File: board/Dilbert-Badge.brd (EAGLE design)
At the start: 106.7 x 52.1 mm, 39 parts, among them IC1 MCP23017SO, J1 IO EXP., J2 FTDI_DEVICE, J3 NEOPIXEL, J5 I2C, SW1 UP, SW2 DOWN, SW3 LEFT, SW4 RIGHT, SW5 A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

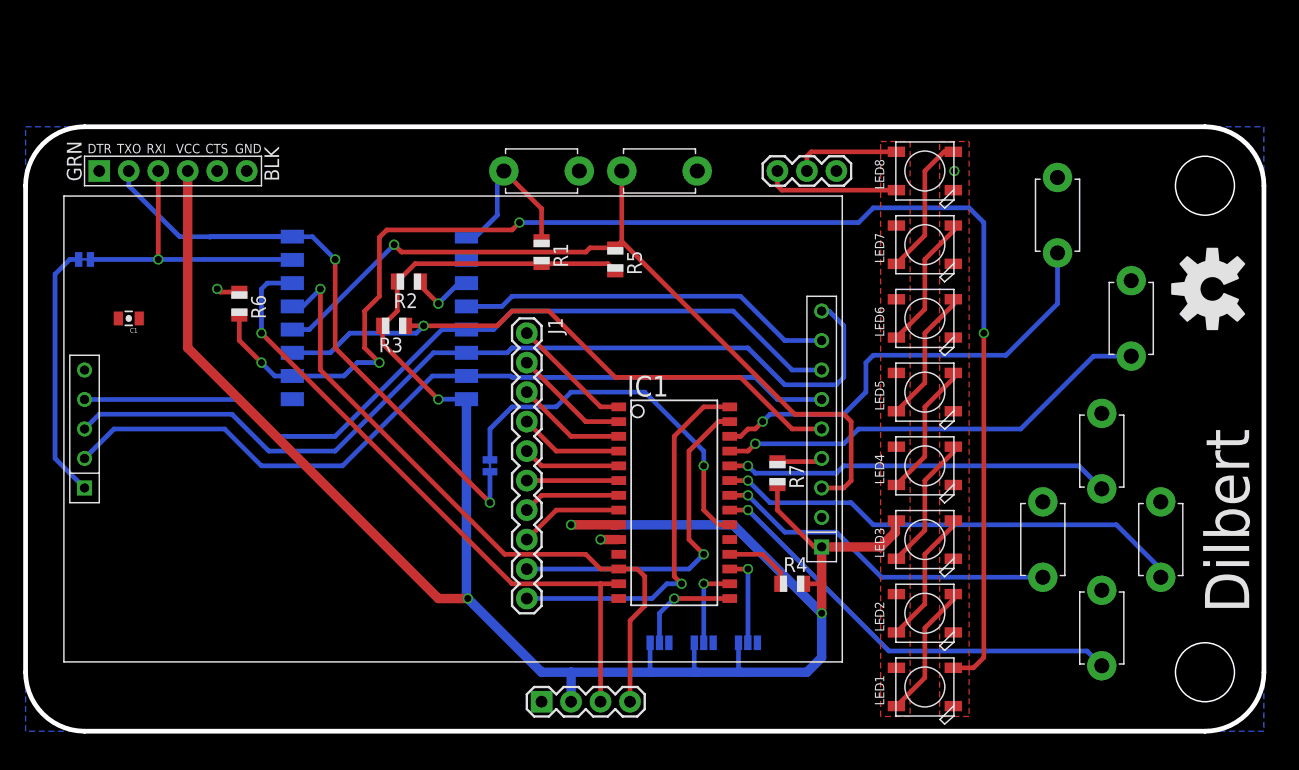
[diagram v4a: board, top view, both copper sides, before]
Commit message: add regulator, tidy layout
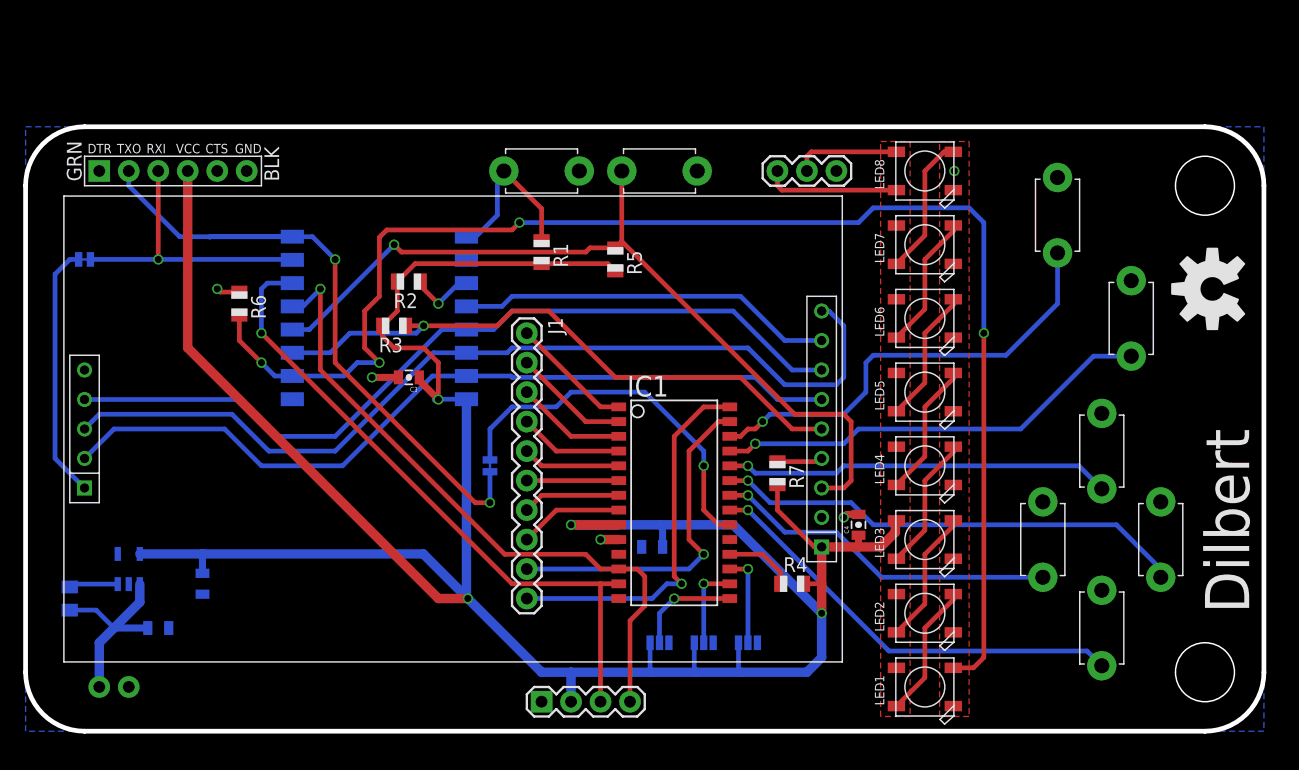
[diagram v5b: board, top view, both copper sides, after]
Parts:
- added C2, C3, C4, C5: 1.0uF, SparkFun-Capacitors:0805-CAP
- added J4: PWR IN, SparkFun-Connectors:1X02
- added R8: 1K, adafruit:R0805
- added U1: 3.3V, SparkFun-PowerIC:SOT23-5
- C1: value (none) -> 1.0uF
- moved C1 26.8 mm to (8.89, 14.0), flipped to the bottom
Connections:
- new net VIN: C1.1, J4.2, R8.2, U1.1
- new net VREG_EN: R8.1, U1.3
- net 3V3: now also C2.1, C3.1, C4.1, C5.1, U1.5; no longer C1.1
- net GND: now also C2.2, C3.2, C4.2, C5.2, J4.1, U1.2
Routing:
- net 3V3: track 208.6 -> 247.5 mm
- net VIN: track 0.00 -> 17.7 mm
- net VREG_EN: track 0.00 -> 4.23 mm
- net GND: track 3.59 -> 7.24 mm, vias 3 -> 5
- net UART_TX: track 58.0 -> 58.7 mm
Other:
- board text added: "VIN"
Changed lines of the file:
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@@
 <text x="49.53" y="9.525" size="1.27" layer="28" rot="MR90" align="center-left">SCL</text>
 <text x="46.99" y="9.525" size="1.27" layer="28" rot="MR90" align="center-left">SDA</text>
+<text x="6.35" y="10.795" size="1.016" layer="28" rot="MR90" align="center-left">GND</text>
+<text x="3.81" y="10.795" size="1.016" layer="28" rot="MR90" align="center-left">VIN</text>
 </plain>
 <attributes>
@@
 </class>
 <class number="1" name="power" width="0.508" drill="0">
+<clearance class="1" value="0.254"/>
 </class>
 </classes>
@@
 <element name="R2" library="adafruit" package="R0805" value="10K" x="30.48" y="43.815" rot="R180"/>
 <element name="R3" library="adafruit" package="R0805" value="10K" x="29.21" y="40.005" rot="R180"/>
-<element name="C1" library="SparkFun-Capacitors" package="0805-CAP" value="" x="6.35" y="40.64" rot="R180">
-<attribute name="PROD_ID" value="CAP-11330" x="6.35" y="40.64" size="1.778" layer="27" rot="R180" display="off"/>
-</element>
 <element name="R5" library="adafruit" package="R0805" value="10K" x="48.26" y="45.72" rot="R270"/>
 <element name="R6" library="adafruit" package="R0805" value="10K" x="15.875" y="41.91" rot="R270"/>
@@
 <attribute name="VALUE" x="60.96" y="56.515" size="1.27" layer="28" rot="MR180"/>
 </element>
+<element name="U1" library="SparkFun-PowerIC" package="SOT23-5" value="3.3V" x="6.35" y="19.05" rot="MR0">
+<attribute name="PROD_ID" value="VREG-12457" x="6.35" y="19.05" size="1.778" layer="28" rot="MR0" display="off"/>
+</element>
+<element name="J4" library="SparkFun-Connectors" package="1X02" value="PWR IN" x="6.35" y="8.89" smashed="yes" rot="MR0">
+<attribute name="VALUE" x="15.24" y="8.255" size="1.27" layer="28" rot="MR0"/>
+</element>
+<element name="R8" library="adafruit" package="R0805" value="1K" x="1.27" y="16.51" rot="MR270"/>
+<element name="C1" library="SparkFun-Capacitors" package="0805-CAP" value="1.0uF" x="8.89" y="13.97" rot="MR180">
+<attribute name="PROD_ID" value="CAP-11625" x="8.89" y="13.97" size="1.016" layer="28" rot="MR180" display="off"/>
+</element>
+<element name="C2" library="SparkFun-Capacitors" package="0805-CAP" value="1.0uF" x="12.7" y="17.78" rot="MR270">
+<attribute name="PROD_ID" value="CAP-11625" x="12.7" y="17.78" size="1.016" layer="28" rot="MR270" display="off"/>
+</element>
+<element name="C3" library="SparkFun-Capacitors" package="0805-CAP" value="1.0uF" x="30.48" y="35.56" rot="R180">
+<attribute name="PROD_ID" value="CAP-11625" x="30.48" y="35.56" size="1.016" layer="27" rot="R180" display="off"/>
+</element>
+<element name="C4" library="SparkFun-Capacitors" package="0805-CAP" value="1.0uF" x="69.215" y="22.86" rot="R90">
+<attribute name="PROD_ID" value="CAP-11625" x="69.215" y="22.86" size="1.016" layer="27" rot="R90" display="off"/>
+</element>
+<element name="C5" library="SparkFun-Capacitors" package="0805-CAP" value="1.0uF" x="51.435" y="20.955" rot="MR0">
+<attribute name="PROD_ID" value="CAP-11625" x="55.245" y="26.035" size="1.016" layer="28" rot="MR0" display="off"/>
+</element>
 </elements>
 <signals>
@@
 <contactref element="IC1" pad="10"/>
 <contactref element="SW8" pad="P$1"/>
-<contactref element="C1" pad="2"/>
 <contactref element="R6" pad="1"/>
 <contactref element="U$1" pad="GND"/>
@@
 <wire x1="14.24" y1="42.91" x2="13.97" y2="43.18" width="0.4064" layer="1"/>
 <via x="13.97" y="43.18" extent="1-16" drill="0.6"/>
-<wire x1="13.97" y1="43.18" x2="5.45" y2="40.64" width="0" layer="19" extent="1-1"/>
+<contactref element="U1" pad="2"/>
+<contactref element="J4" pad="1"/>
+<contactref element="C1" pad="2"/>
+<contactref element="C2" pad="2"/>
+<contactref element="C3" pad="2"/>
+<contactref element="C4" pad="2"/>
+<contactref element="C5" pad="2"/>
+<wire x1="29.58" y1="35.56" x2="27.305" y2="35.56" width="0.6096" layer="1"/>
+<via x="27.305" y="35.56" extent="1-16" drill="0.6"/>
+<wire x1="69.215" y1="23.76" x2="68.21" y2="23.76" width="0.6096" layer="1"/>
+<wire x1="68.21" y1="23.76" x2="67.945" y2="23.495" width="0.6096" layer="1"/>
+<via x="67.945" y="23.495" extent="1-16" drill="0.6"/>
+<wire x1="77.38" y1="7.24" x2="77.38" y2="13.59" width="0" layer="19" extent="1-1"/>
 </signal>
 <signal name="BTN_U">
@@
 <wire x1="22.17" y1="47.68" x2="24.13" y2="45.72" width="0.4064" layer="16"/>
 <via x="24.13" y="45.72" extent="1-16" drill="0.6"/>
-<wire x1="24.13" y1="45.72" x2="24.13" y2="38.1" width="0.4064" layer="1"/>
-<wire x1="24.13" y1="38.1" x2="37.465" y2="24.765" width="0.4064" layer="1"/>
+<wire x1="24.13" y1="45.72" x2="24.13" y2="36.83" width="0.4064" layer="1"/>
 <via x="37.465" y="24.765" extent="1-16" drill="0.6"/>
 <wire x1="37.465" y1="24.765" x2="37.465" y2="27.432" width="0.4064" layer="16"/>
+<wire x1="24.13" y1="36.83" x2="36.195" y2="24.765" width="0.4064" layer="1"/>
+<wire x1="36.195" y1="24.765" x2="37.465" y2="24.765" width="0.4064" layer="1"/>
 </signal>
 <signal name="UART_RX">
@@
 <contactref element="R2" pad="2"/>
 <contactref element="R3" pad="2"/>
-<contactref element="C1" pad="1"/>
 <contactref element="R5" pad="2"/>
 <contactref element="U$1" pad="VCC"/>
@@
 <contactref element="LED7" pad="1-VDD"/>
 <contactref element="LED6" pad="1-VDD"/>
-<wire x1="66.04" y1="20.955" x2="71.12" y2="20.955" width="0.8128" layer="1"/>
+<wire x1="66.04" y1="20.955" x2="69.215" y2="20.955" width="0.8128" layer="1"/>
+<wire x1="69.215" y1="20.955" x2="71.12" y2="20.955" width="0.8128" layer="1"/>
 <wire x1="71.12" y1="20.955" x2="72.39" y2="22.225" width="0.8128" layer="1"/>
 <wire x1="72.39" y1="22.225" x2="72.39" y2="23.15" width="0.8128" layer="1"/>
@@
 <wire x1="66.04" y1="17.78" x2="66.04" y2="15.24" width="0.8128" layer="1"/>
 <wire x1="66.04" y1="15.24" x2="58.42" y2="22.86" width="0.8128" layer="16"/>
-<wire x1="58.42" y1="22.86" x2="44.45" y2="22.86" width="0.8128" layer="16"/>
+<wire x1="58.42" y1="22.86" x2="52.07" y2="22.86" width="0.8128" layer="16"/>
 <via x="44.45" y="22.86" extent="1-16" drill="0.6"/>
+<wire x1="52.07" y1="22.86" x2="44.45" y2="22.86" width="0.8128" layer="16"/>
 <wire x1="44.45" y1="22.86" x2="48.56" y2="22.86" width="0.8128" layer="1"/>
 <wire x1="64.5" y1="17.78" x2="66.04" y2="17.78" width="0.4064" layer="1"/>
@@
 <wire x1="29.48" y1="43.815" x2="29.48" y2="41.275" width="0.4064" layer="1"/>
 <wire x1="29.48" y1="41.275" x2="28.21" y2="40.005" width="0.4064" layer="1"/>
-<wire x1="28.21" y1="40.005" x2="28.21" y2="38.465" width="0.4064" layer="1"/>
-<wire x1="28.21" y1="38.465" x2="33.02" y2="33.655" width="0.4064" layer="1"/>
-<wire x1="11.43" y1="38.1" x2="7.25" y2="40.64" width="0" layer="19" extent="1-1"/>
+<contactref element="U1" pad="5"/>
+<wire x1="7.3" y1="20.3501" x2="12.7" y2="20.3501" width="0.8128" layer="16"/>
+<wire x1="12.7" y1="20.3501" x2="31.7199" y2="20.3501" width="0.8128" layer="16"/>
+<wire x1="31.7199" y1="20.3501" x2="35.56" y2="16.51" width="0.8128" layer="16"/>
+<contactref element="C2" pad="1"/>
+<contactref element="C3" pad="1"/>
+<contactref element="C4" pad="1"/>
+<contactref element="C5" pad="1"/>
+<wire x1="12.7" y1="18.68" x2="12.7" y2="20.3501" width="0.6096" layer="16"/>
+<wire x1="33.02" y1="33.655" x2="32.755" y2="33.655" width="0.6096" layer="16"/>
+<wire x1="28.21" y1="40.005" x2="28.21" y2="39.1" width="0.4064" layer="1"/>
+<wire x1="28.21" y1="39.1" x2="29.21" y2="38.1" width="0.4064" layer="1"/>
+<wire x1="29.21" y1="38.1" x2="31.75" y2="38.1" width="0.4064" layer="1"/>
+<wire x1="31.75" y1="38.1" x2="33.02" y2="36.83" width="0.4064" layer="1"/>
+<wire x1="33.02" y1="36.83" x2="33.02" y2="33.655" width="0.4064" layer="1"/>
+<wire x1="31.38" y1="35.56" x2="31.38" y2="35.295" width="0.6096" layer="1"/>
+<wire x1="31.38" y1="35.295" x2="33.02" y2="33.655" width="0.6096" layer="1"/>
+<wire x1="69.215" y1="21.96" x2="69.215" y2="20.955" width="0.6096" layer="1"/>
+<wire x1="52.335" y1="20.955" x2="52.335" y2="22.595" width="0.6096" layer="16"/>
+<wire x1="52.335" y1="22.595" x2="52.07" y2="22.86" width="0.6096" layer="16"/>
+<wire x1="72.48" y1="48.64" x2="72.48" y2="54.99" width="0" layer="19" extent="1-1"/>
 </signal>
 <signal name="TFT_BL">
@@
 <wire x1="58.42" y1="31.75" x2="57.15" y2="31.75" width="0.4064" layer="1"/>
 </signal>
+<signal name="VIN">
+<contactref element="U1" pad="1"/>
+<contactref element="J4" pad="2"/>
+<contactref element="R8" pad="2"/>
+<contactref element="C1" pad="1"/>
+<wire x1="7.3" y1="17.7499" x2="7.3" y2="16.19" width="0.8128" layer="16"/>
+<wire x1="7.3" y1="16.19" x2="5.08" y2="13.97" width="0.8128" layer="16"/>
+<wire x1="5.08" y1="13.97" x2="3.81" y2="12.7" width="0.8128" layer="16"/>
+<wire x1="3.81" y1="12.7" x2="3.81" y2="8.89" width="0.8128" layer="16"/>
+<wire x1="7.99" y1="13.97" x2="5.08" y2="13.97" width="0.6096" layer="16"/>
+<wire x1="1.27" y1="15.51" x2="3.54" y2="15.51" width="0.4064" layer="16"/>
+<wire x1="3.54" y1="15.51" x2="5.08" y2="13.97" width="0.4064" layer="16"/>
+</signal>
+<signal name="VREG_EN">
+<contactref element="U1" pad="3"/>
+<contactref element="R8" pad="1"/>
+<wire x1="5.4" y1="17.7499" x2="1.5099" y2="17.7499" width="0.4064" layer="16"/>
+<wire x1="1.5099" y1="17.7499" x2="1.27" y2="17.51" width="0.4064" layer="16"/>
+</signal>
 </signals>
